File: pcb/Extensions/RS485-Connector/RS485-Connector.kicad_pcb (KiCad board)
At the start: 2 copper layers, 43 x 17.5 mm, 23 parts, among them J1 Conn_01x08, J2 Conn_01x06, U1 ISOW7841, U2 SN65HVD1470

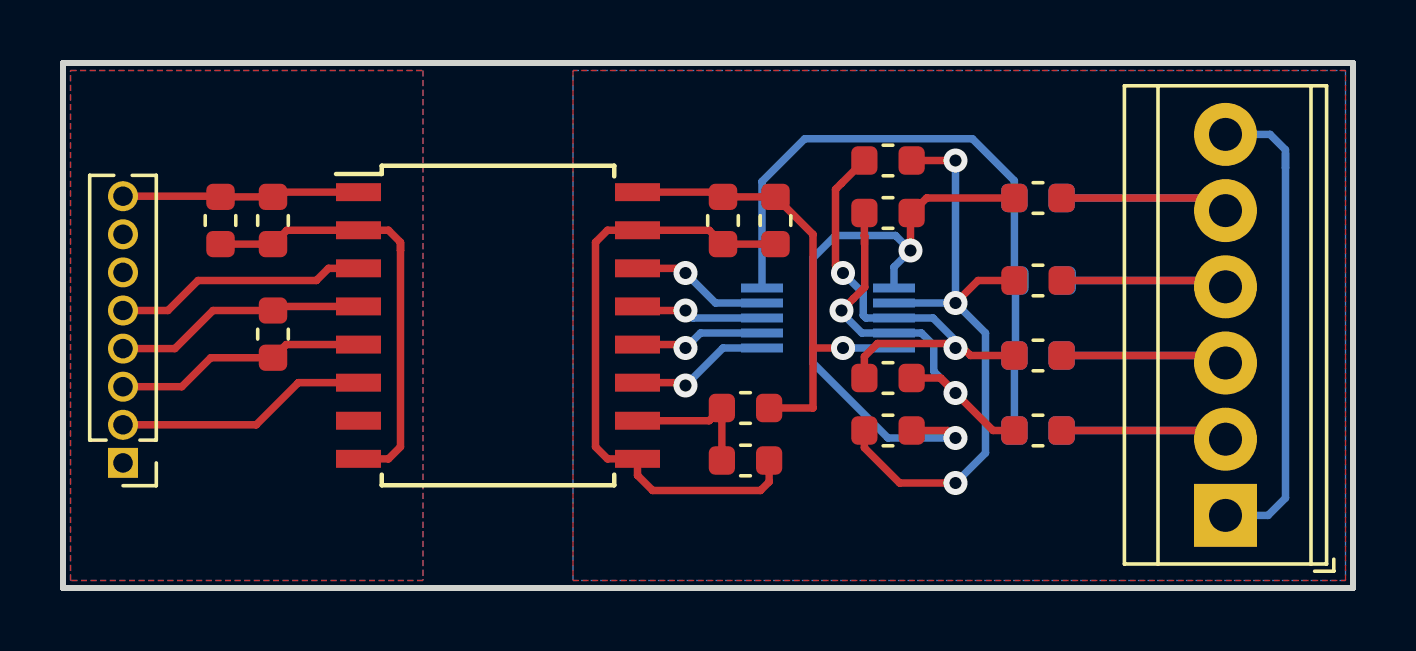
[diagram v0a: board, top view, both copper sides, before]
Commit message: Upgrade RS485 Connector to KiCad 6.0
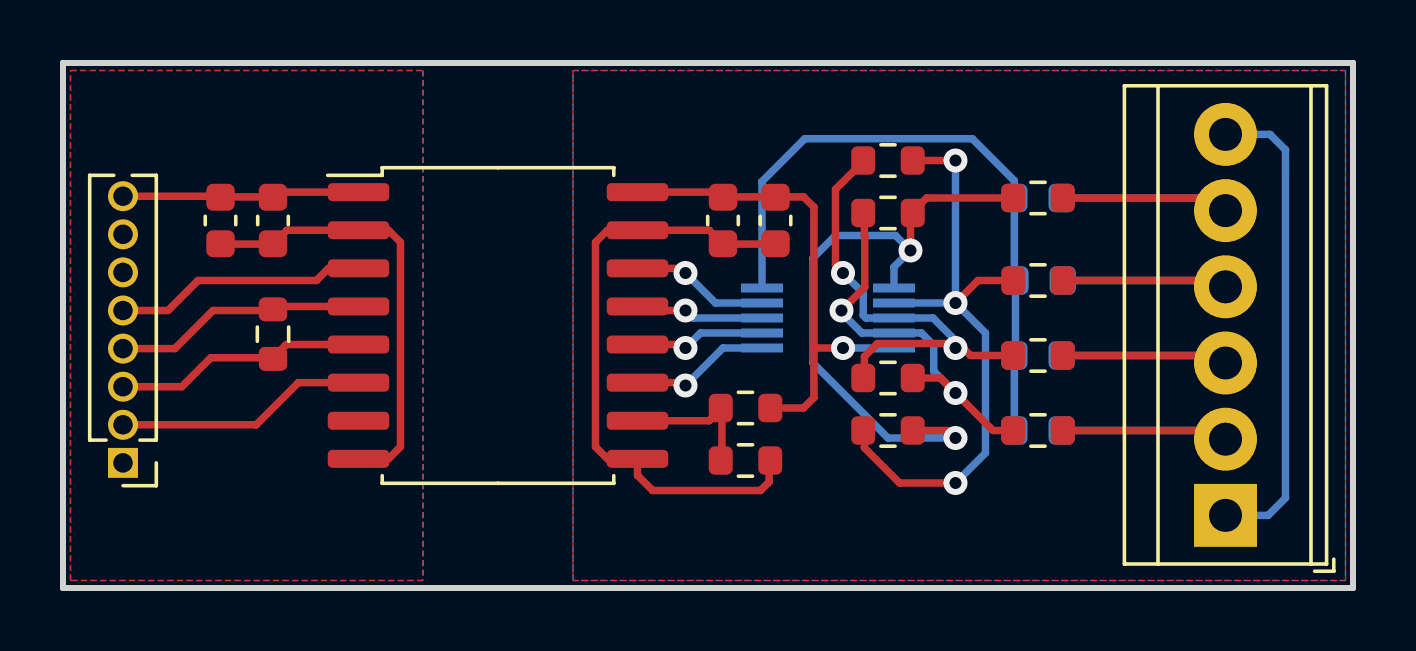
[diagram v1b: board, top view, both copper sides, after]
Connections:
- J1 pad 6: Net-(J1-Pad6) -> unconnected-(J1-Pad6)
- J1 pad 7: Net-(J1-Pad7) -> unconnected-(J1-Pad7)
- U1 pad 7: Net-(U1-Pad7) -> unconnected-(U1-Pad7)
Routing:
- net /Y: track 12.2 -> 10.1 mm
- net GND: track 16.0 -> 14.7 mm
- net /A: track 11.6 -> 10.3 mm
- net /B: track 11.4 -> 10.4 mm
- net /Z: track 11.2 -> 10.5 mm
- net GNDA: track 58.8 -> 58.2 mm
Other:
- net class Default removed
- board text added: "BasilFX 09/2022 V1.1.0"
- board text removed: "BasilFX 08/2018 V1.0.0"
